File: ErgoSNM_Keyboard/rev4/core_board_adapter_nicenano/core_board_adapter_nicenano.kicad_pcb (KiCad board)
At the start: 2 copper layers, 49.5 x 34.3 mm, 12 parts, among them J1 Conn_01x13, J2 Conn_01x03, J3 Conn_01x13, J4 Conn_01x30, J5 Conn_Batt, SW1 SW_DPDT_x2

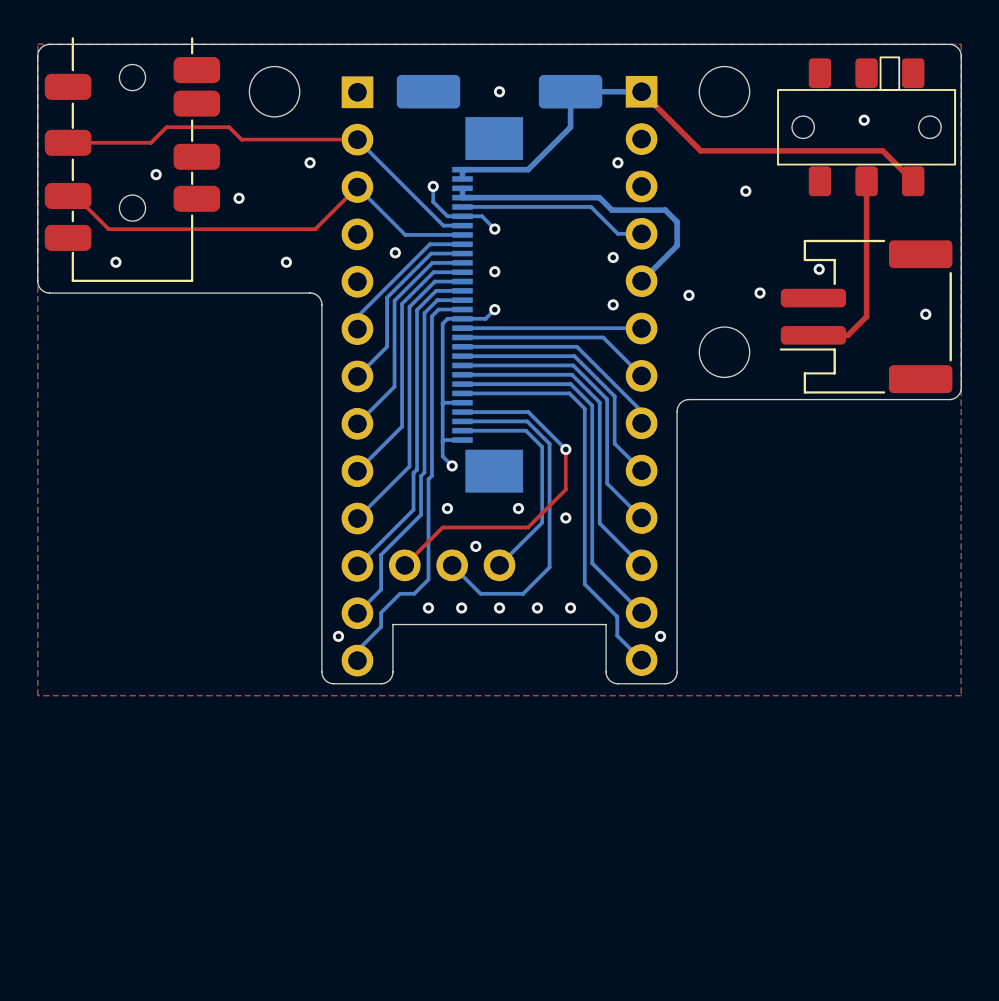
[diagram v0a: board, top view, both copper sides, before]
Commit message: feat: update nice!nano core board
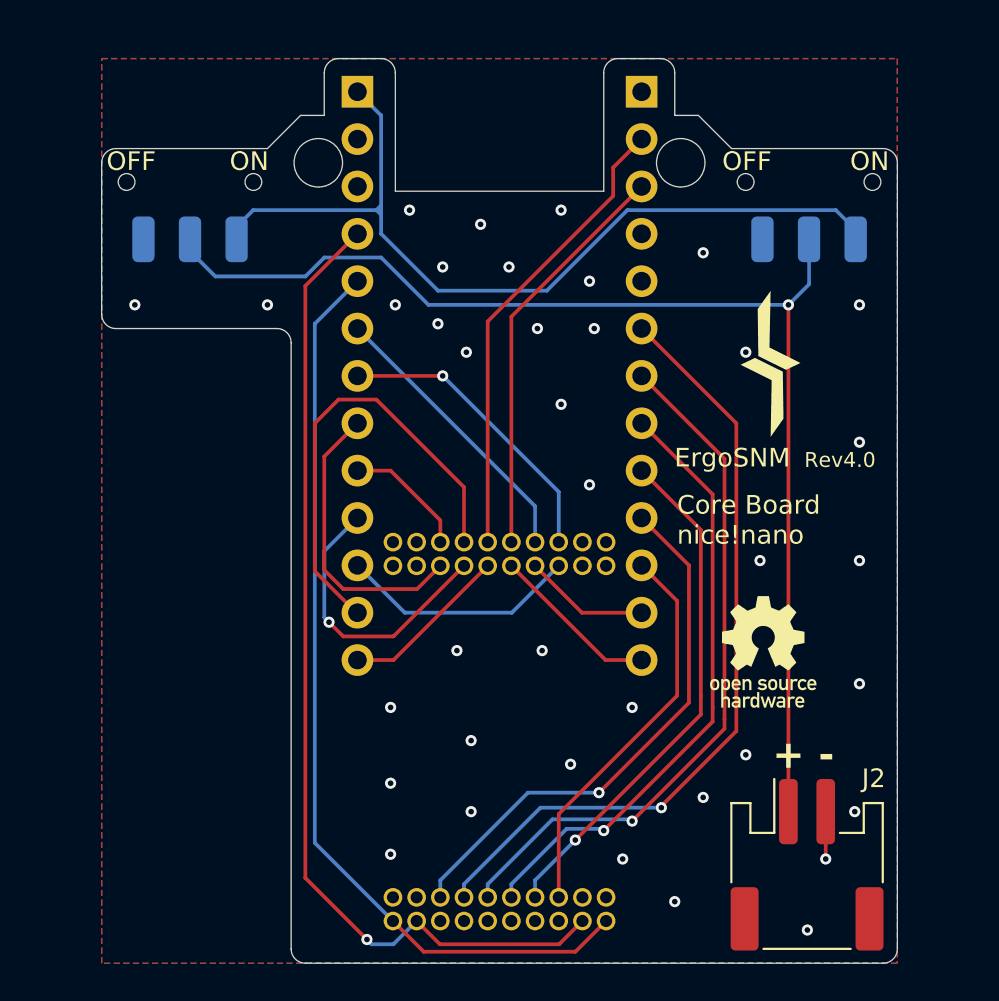
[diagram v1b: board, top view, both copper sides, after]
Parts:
- removed H3: MountingHole, MountingHole:MountingHole_2.7mm_M2.5_ISO7380
- removed TP1: VBAT, TestPoint:TestPoint_Keystone_5015_Micro_Mini
- removed TP2: GND, TestPoint:TestPoint_Keystone_5015_Micro_Mini
- removed TRRS1: PJ-393_TRRS_8P, ErgoSNM_Keyboard:PJ-393 8P TRRS
- added SW2: SW_SPDT, ErgoSNM_Keyboard:9_3.5_3.5_switch, B.Cu at (118.0, 96.3)
- H1, H2: moved to B.Cu
- J2: value Conn_01x03 -> Conn_Batt; footprint Connector_PinHeader_2.54mm:PinHeader_1x03_P2.54mm_Vertical -> Connector_JST:JST_PH_S2B-PH-SM4-TB_1x02-1MP_P2.00mm_Horizontal
- J4: value Conn_01x30 -> Conn_02x10_Odd_Even; footprint Connector_FFC-FPC:TE_3-1734839-0_1x30-1MP_P0.5mm_Horizontal -> Connector_PinHeader_1.27mm:PinHeader_2x10_P1.27mm_Vertical
- J5: value Conn_Batt -> Conn_02x10_Odd_Even; footprint Connector_JST:JST_PH_S2B-PH-SM4-TB_1x02-1MP_P2.00mm_Horizontal -> Connector_PinHeader_1.27mm:PinHeader_2x10_P1.27mm_Vertical; moved to B.Cu
- SW1: value SW_DPDT_x2 -> SW_SPDT; footprint ErgoSNM_Keyboard:MSKT-22D14-T -> ErgoSNM_Keyboard:9_3.5_3.5_switch; moved to B.Cu
- moved J5 35.3 mm to (140.3, 135.9)
- moved J2 26.9 mm to (151.1, 132.9), turned to 0 degrees
- moved J4 15.4 mm to (140.3, 116.9), turned to 90 degrees
- moved J1 15.2 mm to (142.2, 91.4)
- moved J3 15.2 mm to (127.0, 91.4)
- moved H2 4.47 mm to (144.3, 95.2), turned to 180 degrees
- moved H1 4.47 mm to (124.9, 95.2), turned to 180 degrees
- moved SW1 4.26 mm to (151.2, 96.3)
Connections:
- J2 pad 1: P1.01 -> Net-(J2-Pin_1)
- J2 pad 2: P1.02 -> GND
- J4 pad 1: +BATT -> unconnected-(J4-Pin_1-Pad1)
- J4 pad 10: P0.20 -> P0.08
- J4 pad 11: P0.22 -> P0.09
- J4 pad 12: P0.24 -> P0.06
- J4 pad 13: P1.00 -> P1.13
- J4 pad 14: P0.11 -> P0.10
- J4 pad 15: P1.04 -> P0.02
- J4 pad 16: P1.06 -> P1.15
- J4 pad 17: GND -> unconnected-(J4-Pin_17-Pad17)
- J4 pad 18: P0.31 -> unconnected-(J4-Pin_18-Pad18)
- J4 pad 19: P0.29 -> unconnected-(J4-Pin_19-Pad19)
- J4 pad 2: +BATT -> unconnected-(J4-Pin_2-Pad2)
- J4 pad 20: P0.02 -> unconnected-(J4-Pin_20-Pad20)
- J4 pad 3: +3.3V -> unconnected-(J4-Pin_3-Pad3)
- J4 pad 4: +3.3V -> unconnected-(J4-Pin_4-Pad4)
- J4 pad 5: RESET -> P1.11
- J4 pad 6: GND -> P0.29
- J4 pad 7: P0.06 -> P1.04
- J4 pad 8: P0.08 -> P0.31
- J4 pad 9: P0.17 -> P1.06
- J5 pad 1: Net-(J5-Pin_1) -> +3.3V
- SW1 pad 2: Net-(J5-Pin_1) -> Net-(J2-Pin_1)
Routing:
- net Net-(J2-Pin_1): track 0.00 -> 65.9 mm, vias 0 -> 1
- net RESET: track 10.2 -> 53.6 mm, vias 0 -> 1
- net P0.17: track 7.91 -> 42.5 mm, vias 0 -> 1
- net +3.3V: track 16.5 -> 49.8 mm
- net P0.20: track 9.91 -> 37.7 mm, vias 0 -> 1
- net P0.22: track 11.9 -> 32.8 mm, vias 0 -> 1
- net P1.01: track 18.8 -> 0.00 mm, vias 1 -> 0
- net P1.02: track 18.2 -> 0.00 mm
- net +BATT: track 29.5 -> 47.1 mm
- net GND: track 18.0 -> 2.54 mm, vias 32 -> 38
- net P0.24: track 13.9 -> 27.9 mm, vias 0 -> 1
- net P1.06: track 22.4 -> 9.08 mm
- net P1.00: track 15.9 -> 29.2 mm, vias 0 -> 1
- net P1.04: track 19.9 -> 6.76 mm
- net P0.09: track 21.6 -> 9.08 mm
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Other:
- board size 49.5 x 34.3 mm -> 42.7 x 48.5 mm
- board text added: "+"
- board text added: "-"
- board text added: "Core Board nice!nano"
- board text added: "ErgoSNM"
- board text added: "OFF"
- board text added: "ON"
- board text added: "Rev${REVISION}"
